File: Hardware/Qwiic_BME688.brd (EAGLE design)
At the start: 25.4 x 25.4 mm, 35 parts, among them J1 DNP, J2 QWIIC_RA, J4 QWIIC_RA

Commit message: Create BME688 eagle footprint and schematic symbol
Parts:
- added U1: BME688LGA, BME688:LGA_8PIN
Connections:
- new net CSB: U1.2
- new net SDO: U1.5
- new net VDD: U1.8
- new net VDDIO: U1.6
- net GND: now also U1.1, U1.7
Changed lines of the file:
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@@
 <element name="U$5" library="output" package="PWR0" value="" x="0.762" y="7.747" smashed="yes"/>
 <element name="U$6" library="output" package="#PWR#0" value="" x="5.715" y="6.35" smashed="yes" rot="MR0"/>
+<element name="U1" library="BME688" package="LGA_8PIN" value="BME688LGA" x="-15.24" y="-10.16" smashed="yes">
+<attribute name="NAME" x="-16.51" y="-12.7" size="0.635" layer="25" font="vector"/>
+<attribute name="VALUE" x="-16.51" y="-7.62" size="0.635" layer="27" font="vector"/>
+</element>
 </elements>
 <signals>
@@
 <contactref element="J1" pad="1"/>
 <via x="1.016" y="6.35" extent="1-16" drill="0.3"/>
+<contactref element="U1" pad="7"/>
+<contactref element="U1" pad="1"/>
 <wire x1="8.89" y1="1.27" x2="20.32" y2="11.2" width="0" layer="19" extent="1-1"/>
 <wire x1="2.298" y1="6.35" x2="8.89" y2="1.27" width="0" layer="19" extent="1-1"/>
 <wire x1="1.016" y1="6.35" x2="2.298" y2="6.35" width="0" layer="19" extent="1-1"/>
 <wire x1="5.08" y1="14.2" x2="2.298" y2="6.35" width="0" layer="19" extent="1-1"/>
+<wire x1="-14.04" y1="-8.96" x2="1.016" y2="6.35" width="0" layer="19" extent="1-1"/>
+<wire x1="-16.44" y1="-9.76" x2="-14.04" y2="-8.96" width="0" layer="19" extent="1-1"/>
 </signal>
 <signal name="SCL">
@@
 <wire x1="16.256" y1="16.598" x2="13.7414" y2="17.78" width="0" layer="19" extent="1-16"/>
 </signal>
+<signal name="CSB">
+<contactref element="U1" pad="2"/>
+</signal>
+<signal name="SDO">
+<contactref element="U1" pad="5"/>
+</signal>
+<signal name="VDDIO">
+<contactref element="U1" pad="6"/>
+</signal>
+<signal name="VDD">
+<contactref element="U1" pad="8"/>
+</signal>
 </signals>

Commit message: Schematic done
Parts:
- added C1, C2: 0.1uF, SparkFun-Capacitors:0402
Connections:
- removed net CSB: U1.2
- removed net SDO: U1.5
- removed net VDD: U1.8
- removed net VDDIO: U1.6
- net 3.3V: now also C1.1, C2.1, U1.2, U1.6, U1.8
- net GND: now also C1.2, C2.2, U1.5
- net SCL: now also U1.4
- net SDA: now also U1.3
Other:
- board text added: "Priyanka Makin"
- board text removed: "Paul Clark"
- board text removed: "Revised by: Priyanka Makin"
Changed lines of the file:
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@@
 <layer number="56" name="wert" color="7" fill="1" visible="no" active="no"/>
 <layer number="57" name="tCAD" color="7" fill="1" visible="no" active="no"/>
+<layer number="58" name="bCopper" color="7" fill="1" visible="no" active="no"/>
 <layer number="59" name="tCarbon" color="7" fill="1" visible="no" active="no"/>
 <layer number="60" name="bCarbon" color="7" fill="1" visible="no" active="no"/>
@@
 <layer number="250" name="Descript" color="3" fill="1" visible="no" active="no"/>
 <layer number="251" name="SMDround" color="12" fill="11" visible="no" active="no"/>
+<layer number="253" name="Extra" color="7" fill="1" visible="no" active="no"/>
 <layer number="254" name="cooling" color="7" fill="1" visible="no" active="no"/>
 <layer number="255" name="routoute" color="7" fill="1" visible="no" active="no"/>
@@
 <dimension x1="0" y1="25.4" x2="25.4" y2="25.4" x3="12.7" y3="34.29" textsize="1.778" textratio="15" layer="47" unit="inch"/>
 <text x="12.7" y="39.37" size="1.778" layer="47" font="vector" ratio="15" align="center">Dimensions in inches</text>
-<text x="76.2" y="-10.16" size="1.778" layer="51" font="vector" ratio="10">Paul Clark</text>
+<text x="76.2" y="-10.16" size="1.778" layer="51" font="vector" ratio="10">Priyanka Makin</text>
 <text x="33.02" y="38.1" size="1.778" layer="51" font="vector" ratio="10" align="top-left">2 Layers
 1.6mm Thickness
 HASL Finish</text>
-<text x="57.15" y="-12.7" size="1.778" layer="51" font="vector" ratio="10">Revised by: Priyanka Makin</text>
 <dimension x1="5.08" y1="12.7" x2="5.08" y2="0" x3="-1.27" y3="6.35" textsize="1.778" textratio="15" layer="47" unit="inch"/>
 <dimension x1="8.89" y1="1.27" x2="0" y2="1.27" x3="4.445" y3="26.67" textsize="1.778" textratio="15" layer="47" unit="inch"/>
@@
 <attribute name="VALUE" x="-16.51" y="-7.62" size="0.635" layer="27" font="vector"/>
 </element>
+<element name="C1" library="SparkFun-Capacitors" package="0402" value="0.1uF" x="-13.97" y="-15.24" smashed="yes">
+<attribute name="NAME" x="-13.97" y="-14.478" size="0.6096" layer="25" font="vector" ratio="20" align="bottom-center"/>
+<attribute name="PROD_ID" value="CAP-12416" x="-13.97" y="-15.24" size="1.778" layer="27" font="vector" ratio="15" display="off"/>
+<attribute name="VALUE" x="-13.97" y="-16.002" size="0.6096" layer="27" font="vector" ratio="20" align="top-center"/>
+</element>
+<element name="C2" library="SparkFun-Capacitors" package="0402" value="0.1uF" x="-13.97" y="-19.05" smashed="yes">
+<attribute name="NAME" x="-13.97" y="-18.288" size="0.6096" layer="25" font="vector" ratio="20" align="bottom-center"/>
+<attribute name="PROD_ID" value="CAP-12416" x="-13.97" y="-19.05" size="1.778" layer="27" font="vector" ratio="15" display="off"/>
+<attribute name="VALUE" x="-13.97" y="-19.812" size="0.6096" layer="27" font="vector" ratio="20" align="top-center"/>
+</element>
 </elements>
 <signals>
@@
 <contactref element="I2C" pad="2"/>
 <wire x1="20.328" y1="12.192" x2="20.32" y2="12.2" width="0.4064" layer="1"/>
+<contactref element="U1" pad="6"/>
+<contactref element="U1" pad="8"/>
+<contactref element="U1" pad="2"/>
+<contactref element="C1" pad="1"/>
+<contactref element="C2" pad="1"/>
 <wire x1="5.08" y1="13.2" x2="12.7" y2="17.78" width="0" layer="19" extent="1-16"/>
 <wire x1="6.0833" y1="6.35" x2="5.08" y2="13.2" width="0" layer="19" extent="1-16"/>
 <wire x1="11.43" y1="1.27" x2="6.0833" y2="6.35" width="0" layer="19" extent="16-16"/>
 <wire x1="20.32" y1="12.2" x2="12.7" y2="17.78" width="0" layer="19" extent="1-16"/>
+<wire x1="-14.04" y1="-9.76" x2="6.0833" y2="6.35" width="0" layer="19" extent="1-16"/>
+<wire x1="-16.44" y1="-10.56" x2="-14.04" y2="-9.76" width="0" layer="19" extent="1-1"/>
+<wire x1="-16.44" y1="-8.96" x2="-16.44" y2="-10.56" width="0" layer="19" extent="1-1"/>
+<wire x1="-14.55" y1="-15.24" x2="-16.44" y2="-10.56" width="0" layer="19" extent="1-1"/>
+<wire x1="-14.55" y1="-19.05" x2="-14.55" y2="-15.24" width="0" layer="19" extent="1-1"/>
 </signal>
 <signal name="GND">
@@
 <contactref element="J1" pad="1"/>
 <via x="1.016" y="6.35" extent="1-16" drill="0.3"/>
+<contactref element="U1" pad="5"/>
 <contactref element="U1" pad="7"/>
 <contactref element="U1" pad="1"/>
+<contactref element="C1" pad="2"/>
+<contactref element="C2" pad="2"/>
 <wire x1="8.89" y1="1.27" x2="20.32" y2="11.2" width="0" layer="19" extent="1-1"/>
 <wire x1="2.298" y1="6.35" x2="8.89" y2="1.27" width="0" layer="19" extent="1-1"/>
@@
 <wire x1="-14.04" y1="-8.96" x2="1.016" y2="6.35" width="0" layer="19" extent="1-1"/>
 <wire x1="-16.44" y1="-9.76" x2="-14.04" y2="-8.96" width="0" layer="19" extent="1-1"/>
+<wire x1="-16.44" y1="-11.36" x2="-16.44" y2="-9.76" width="0" layer="19" extent="1-1"/>
+<wire x1="-13.39" y1="-15.24" x2="-16.44" y2="-11.36" width="0" layer="19" extent="1-1"/>
+<wire x1="-13.39" y1="-19.05" x2="-13.39" y2="-15.24" width="0" layer="19" extent="1-1"/>
 </signal>
 <signal name="SCL">
@@
 <contactref element="R2" pad="1"/>
 <contactref element="J1" pad="4"/>
+<contactref element="U1" pad="4"/>
 <wire x1="16.256" y1="14.898" x2="20.32" y2="14.2" width="0" layer="19" extent="1-1"/>
 <wire x1="5.08" y1="11.2" x2="16.256" y2="14.898" width="0" layer="19" extent="1-1"/>
 <wire x1="16.51" y1="1.27" x2="20.32" y2="14.2" width="0" layer="19" extent="1-1"/>
+<wire x1="-14.04" y1="-11.36" x2="5.08" y2="11.2" width="0" layer="19" extent="1-1"/>
 </signal>
 <signal name="SDA">
@@
 <contactref element="J1" pad="3"/>
 <wire x1="9.144" y1="14.898" x2="9.1349375" y2="14.9070625" width="0.3048" layer="1"/>
+<contactref element="U1" pad="3"/>
 <wire x1="9.144" y1="14.898" x2="20.32" y2="13.2" width="0" layer="19" extent="1-1"/>
 <wire x1="5.08" y1="12.2" x2="9.144" y2="14.898" width="0" layer="19" extent="1-1"/>
 <wire x1="13.97" y1="1.27" x2="20.32" y2="13.2" width="0" layer="19" extent="1-1"/>
+<wire x1="-14.04" y1="-10.56" x2="5.08" y2="12.2" width="0" layer="19" extent="1-1"/>
 </signal>
 <signal name="N$3">
@@
 <wire x1="16.256" y1="16.598" x2="13.7414" y2="17.78" width="0" layer="19" extent="1-16"/>
 </signal>
-<signal name="CSB">
-<contactref element="U1" pad="2"/>
-</signal>
-<signal name="SDO">
-<contactref element="U1" pad="5"/>
-</signal>
-<signal name="VDDIO">
-<contactref element="U1" pad="6"/>
-</signal>
-<signal name="VDD">
-<contactref element="U1" pad="8"/>
-</signal>
 </signals>

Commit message: Updating schematic
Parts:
- added ADR: JUMPER-SMT_3_1-NC_TRACE_SILK, SparkFun-Jumpers:SMT-JUMPER_3_1-NC_TRACE_SILK
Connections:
- new net N$6: ADR.2, U1.5
- net 3.3V: now also ADR.1
- net GND: now also ADR.3; no longer U1.5
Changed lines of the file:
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@@
 <attribute name="VALUE" x="-13.97" y="-19.812" size="0.6096" layer="27" font="vector" ratio="20" align="top-center"/>
+</element>
+<element name="ADR" library="SparkFun-Jumpers" package="SMT-JUMPER_3_1-NC_TRACE_SILK" package3d_urn="urn:adsk.eagle:package:39288/1" value="JUMPER-SMT_3_1-NC_TRACE_SILK" x="-19.05" y="-17.78" smashed="yes">
+<attribute name="NAME" x="-19.05" y="-16.637" size="0.6096" layer="25" font="vector" ratio="20" align="bottom-center"/>
+<attribute name="VALUE" x="-19.05" y="-18.923" size="0.6096" layer="27" font="vector" ratio="20" align="top-center"/>
 </element>
 </elements>
@@
 <contactref element="C1" pad="1"/>
 <contactref element="C2" pad="1"/>
-<wire x1="5.08" y1="13.2" x2="12.7" y2="17.78" width="0" layer="19" extent="1-16"/>
-<wire x1="6.0833" y1="6.35" x2="5.08" y2="13.2" width="0" layer="19" extent="1-16"/>
+<contactref element="ADR" pad="1"/>
+<wire x1="-14.55" y1="-19.05" x2="-20.0914" y2="-17.78" width="0" layer="19" extent="1-1"/>
+<wire x1="-14.55" y1="-15.24" x2="-14.55" y2="-19.05" width="0" layer="19" extent="1-1"/>
+<wire x1="-16.44" y1="-10.56" x2="-14.55" y2="-15.24" width="0" layer="19" extent="1-1"/>
+<wire x1="-16.44" y1="-8.96" x2="-16.44" y2="-10.56" width="0" layer="19" extent="1-1"/>
+<wire x1="-14.04" y1="-9.76" x2="-16.44" y2="-10.56" width="0" layer="19" extent="1-1"/>
+<wire x1="6.0833" y1="6.35" x2="-14.04" y2="-9.76" width="0" layer="19" extent="1-16"/>
+<wire x1="5.08" y1="13.2" x2="6.0833" y2="6.35" width="0" layer="19" extent="1-16"/>
 <wire x1="11.43" y1="1.27" x2="6.0833" y2="6.35" width="0" layer="19" extent="16-16"/>
+<wire x1="12.7" y1="17.78" x2="5.08" y2="13.2" width="0" layer="19" extent="1-16"/>
 <wire x1="20.32" y1="12.2" x2="12.7" y2="17.78" width="0" layer="19" extent="1-16"/>
-<wire x1="-14.04" y1="-9.76" x2="6.0833" y2="6.35" width="0" layer="19" extent="1-16"/>
-<wire x1="-16.44" y1="-10.56" x2="-14.04" y2="-9.76" width="0" layer="19" extent="1-1"/>
-<wire x1="-16.44" y1="-8.96" x2="-16.44" y2="-10.56" width="0" layer="19" extent="1-1"/>
-<wire x1="-14.55" y1="-15.24" x2="-16.44" y2="-10.56" width="0" layer="19" extent="1-1"/>
-<wire x1="-14.55" y1="-19.05" x2="-14.55" y2="-15.24" width="0" layer="19" extent="1-1"/>
 </signal>
 <signal name="GND">
@@
 <contactref element="J1" pad="1"/>
 <via x="1.016" y="6.35" extent="1-16" drill="0.3"/>
-<contactref element="U1" pad="5"/>
+<contactref element="C1" pad="2"/>
+<contactref element="C2" pad="2"/>
+<contactref element="ADR" pad="3"/>
 <contactref element="U1" pad="7"/>
 <contactref element="U1" pad="1"/>
-<contactref element="C1" pad="2"/>
-<contactref element="C2" pad="2"/>
-<wire x1="8.89" y1="1.27" x2="20.32" y2="11.2" width="0" layer="19" extent="1-1"/>
-<wire x1="2.298" y1="6.35" x2="8.89" y2="1.27" width="0" layer="19" extent="1-1"/>
-<wire x1="1.016" y1="6.35" x2="2.298" y2="6.35" width="0" layer="19" extent="1-1"/>
+<wire x1="-13.39" y1="-19.05" x2="-18.0086" y2="-17.78" width="0" layer="19" extent="1-1"/>
+<wire x1="-13.39" y1="-15.24" x2="-13.39" y2="-19.05" width="0" layer="19" extent="1-1"/>
+<wire x1="-16.44" y1="-9.76" x2="-13.39" y2="-15.24" width="0" layer="19" extent="1-1"/>
+<wire x1="-14.04" y1="-8.96" x2="-16.44" y2="-9.76" width="0" layer="19" extent="1-1"/>
+<wire x1="1.016" y1="6.35" x2="-14.04" y2="-8.96" width="0" layer="19" extent="1-1"/>
+<wire x1="2.298" y1="6.35" x2="1.016" y2="6.35" width="0" layer="19" extent="1-1"/>
 <wire x1="5.08" y1="14.2" x2="2.298" y2="6.35" width="0" layer="19" extent="1-1"/>
-<wire x1="-14.04" y1="-8.96" x2="1.016" y2="6.35" width="0" layer="19" extent="1-1"/>
-<wire x1="-16.44" y1="-9.76" x2="-14.04" y2="-8.96" width="0" layer="19" extent="1-1"/>
-<wire x1="-16.44" y1="-11.36" x2="-16.44" y2="-9.76" width="0" layer="19" extent="1-1"/>
-<wire x1="-13.39" y1="-15.24" x2="-16.44" y2="-11.36" width="0" layer="19" extent="1-1"/>
-<wire x1="-13.39" y1="-19.05" x2="-13.39" y2="-15.24" width="0" layer="19" extent="1-1"/>
+<wire x1="8.89" y1="1.27" x2="2.298" y2="6.35" width="0" layer="19" extent="1-1"/>
+<wire x1="20.32" y1="11.2" x2="8.89" y2="1.27" width="0" layer="19" extent="1-1"/>
 </signal>
 <signal name="SCL">
@@
 <wire x1="16.256" y1="16.598" x2="13.7414" y2="17.78" width="0" layer="19" extent="1-16"/>
 </signal>
+<signal name="N$6">
+<contactref element="U1" pad="5"/>
+<contactref element="ADR" pad="2"/>
+<wire x1="-16.44" y1="-11.36" x2="-19.05" y2="-17.78" width="0" layer="19" extent="1-1"/>
+</signal>
 </signals>

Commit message: Board routed
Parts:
- C1, C2: device SparkFun-Capacitors:0402 -> SparkFun-Capacitors:0603
- moved C2 42.0 mm to (10.2, 15.3), turned to 90 degrees
- moved ADR 40.5 mm to (11.4, 8.89), flipped to the bottom, turned to 180 degrees
- moved U1 36.1 mm to (12.7, 12.7)
- moved C1 35.8 mm to (8.89, 12.3), turned to 180 degrees
- moved R1 8.98 mm to (18.0, 17.0)
- moved I2C 5.12 mm to (17.1, 20.3), turned to 180 degrees
- moved R2 1.27 mm to (16.3, 17.0)
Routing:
- net 3.3V: track 0.01 -> 57.4 mm, vias 0 -> 3
- net SDA: track 0.01 -> 38.8 mm, vias 0 -> 2
- net SCL: track 0.00 -> 35.4 mm, vias 0 -> 3
- net N$1: track 0.00 -> 2.95 mm, vias 0 -> 1
- net N$6: track 0.00 -> 2.64 mm, vias 0 -> 1
- net N$4: track 0.00 -> 2.52 mm, vias 0 -> 1
- net N$2: track 0.00 -> 2.52 mm, vias 0 -> 1

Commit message: Buzzard labels
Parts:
- added U$10, U$7: (no value), output:GAS_SENSOR_#_BME6880
- added U$11: (no value), output:#ADR#0
- added U$9: (no value), output:ADR#_0X760
- moved U$15 5.06 mm to (19.1, 18.3)
- moved LOGO4 3.94 mm to (7.11, 23.9)
- moved LOGO3 2.97 mm to (13.7, 23.1)
- moved LOGO2 0.40 mm to (22.6, 17.4)
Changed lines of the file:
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@@
 <?xml version="1.0" encoding="utf-8"?>
 <!DOCTYPE eagle SYSTEM "eagle.dtd">
-<eagle version="9.5.2">
+<eagle version="9.6.2">
 <drawing>
 <settings>
-<setting alwaysvectorfont="no"/>
+<setting alwaysvectorfont="yes"/>
 <setting keepoldvectorfont="yes"/>
 <setting verticaltext="up"/>
@@
 <layer number="19" name="Unrouted" color="6" fill="1" visible="yes" active="yes"/>
 <layer number="20" name="Dimension" color="24" fill="1" visible="yes" active="yes"/>
-<layer number="21" name="tPlace" color="16" fill="1" visible="yes" active="yes"/>
+<layer number="21" name="tPlace" color="16" fill="1" visible="no" active="yes"/>
 <layer number="22" name="bPlace" color="14" fill="1" visible="yes" active="yes"/>
 <layer number="23" name="tOrigins" color="15" fill="1" visible="yes" active="yes"/>
@@
 <attribute name="NAME" x="17.145" y="19.177" size="0.6096" layer="26" font="vector" ratio="20" rot="MR180" align="bottom-center"/>
 </element>
-<element name="U$15" library="SparkFun-Buzzard" package="I2C" value="" x="14.605" y="15.875" smashed="yes" rot="MR0"/>
+<element name="U$15" library="SparkFun-Buzzard" package="I2C" value="" x="19.05" y="18.288" smashed="yes" rot="MR0"/>
 <element name="LOGO1" library="SparkFun-Aesthetics" package="ORDERING_INSTRUCTIONS" value="SPECIAL_INSTRUCTIONS-ORDERING" x="30.48" y="50.8" smashed="yes"/>
 <element name="U$33" library="output" package="#GND#0" value="" x="8.89" y="3.937" smashed="yes" rot="R90"/>
@@
 <element name="U$3" library="output" package="#SDA#0" value="" x="13.97" y="1.778" smashed="yes" rot="MR90"/>
 <element name="U$4" library="output" package="#SCL#0" value="" x="16.51" y="1.778" smashed="yes" rot="MR90"/>
-<element name="LOGO2" library="SparkFun-Aesthetics" package="QWIIC_5MM" value="QWIIC_LOGO_5MM" x="22.479" y="17.78" smashed="yes"/>
-<element name="LOGO3" library="SparkFun-Aesthetics" package="SFE_LOGO_NAME_.1" value="SFE_LOGO_NAME.1_INCH" x="12.7" y="20.32" smashed="yes" rot="MR0"/>
-<element name="LOGO4" library="SparkFun-Aesthetics" package="SFE_LOGO_FLAME_.1" value="SFE_LOGO_FLAME.1_INCH" x="10.922" y="22.86" smashed="yes" rot="MR0"/>
+<element name="LOGO2" library="SparkFun-Aesthetics" package="QWIIC_5MM" value="QWIIC_LOGO_5MM" x="22.606" y="17.399" smashed="yes"/>
+<element name="LOGO3" library="SparkFun-Aesthetics" package="SFE_LOGO_NAME_.1" value="SFE_LOGO_NAME.1_INCH" x="13.716" y="23.114" smashed="yes" rot="MR0"/>
+<element name="LOGO4" library="SparkFun-Aesthetics" package="SFE_LOGO_FLAME_.1" value="SFE_LOGO_FLAME.1_INCH" x="7.112" y="23.876" smashed="yes" rot="MR0"/>
 <element name="LOGO6" library="SparkFun-Aesthetics" package="SFE_LOGO_NAME_.1" value="SFE_LOGO_NAME.1_INCH" x="12.7" y="23.368" smashed="yes"/>
 <element name="JP7" library="SparkFun-Hardware" package="STAND-OFF" value="STAND-OFF" x="22.86" y="2.54" smashed="yes">
@@
 <attribute name="VALUE" x="11.43" y="10.033" size="0.6096" layer="28" font="vector" ratio="20" rot="MR180" align="top-center"/>
 </element>
+<element name="U$9" library="output" package="ADR#_0X760" value="" x="8.255" y="19.939" smashed="yes"/>
+<element name="U$10" library="output" package="GAS_SENSOR_#_BME6880" value="" x="4.445" y="21.336" smashed="yes"/>
+<element name="U$11" library="output" package="#ADR#0" value="" x="10.16" y="8.89" smashed="yes" rot="MR0"/>
+<element name="U$7" library="output" package="GAS_SENSOR_#_BME6880" value="" x="20.32" y="13.97" smashed="yes" rot="MR0"/>
 </elements>
 <signals>

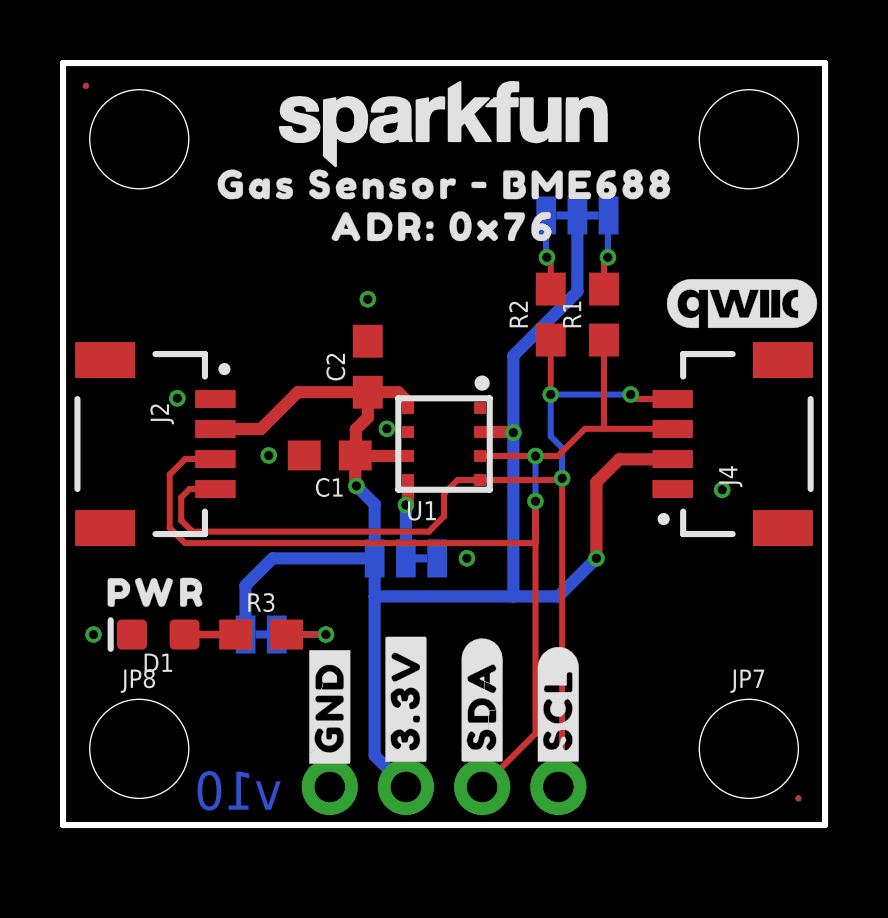
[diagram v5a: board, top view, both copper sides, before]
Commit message: Design review updates
Schematic:
* Add headers for CSB and SDO
* Add NC jumper between CSB and 3.3V
* Add 10k resistor for 3-way jumper
* Replace I2C pullups with 2.2kohms
* Increase the size of fiducials
Board:
* Change version number to v01
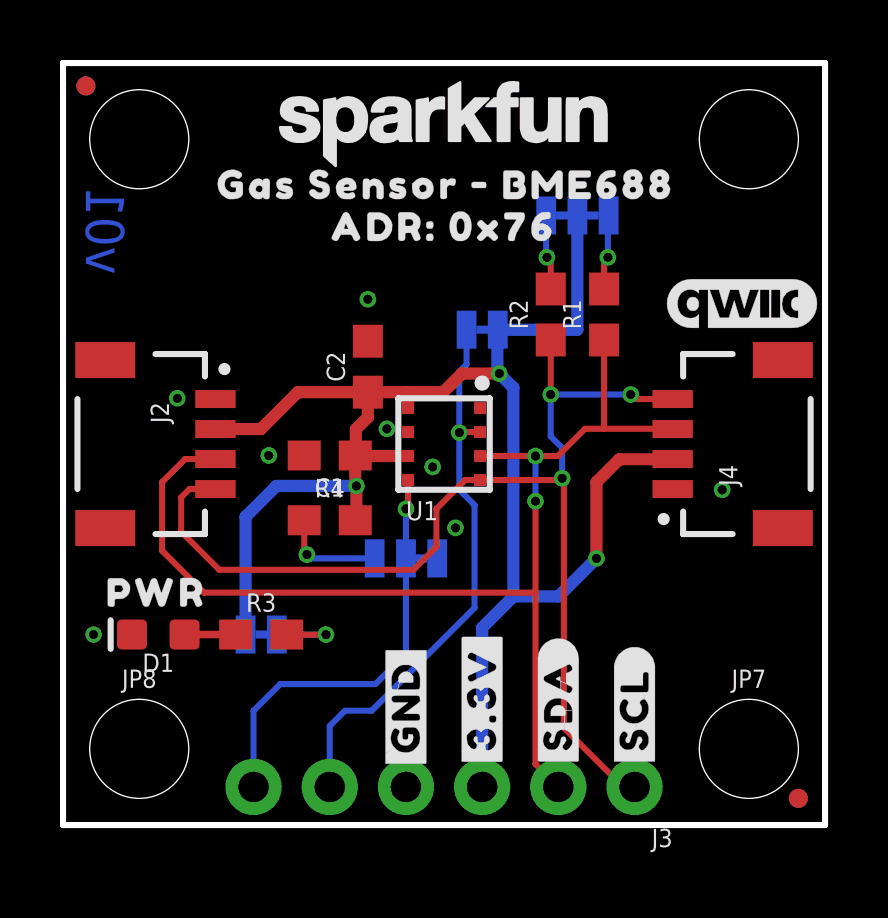
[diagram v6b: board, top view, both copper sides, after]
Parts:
- removed J1: DNP, SparkFun-Connectors:1X04_NO_SILK
- added CSB: JUMPER-SMT_2_NC_TRACE_SILK, SparkFun-Jumpers:SMT-JUMPER_2_NC_TRACE_SILK
- added J3: (no value), SparkFun-Connectors:1X06_NO_SILK
- added R4: 10k, SparkFun-Resistors:0603
- JP1, JP2, JP5, JP6: value FIDUCIAL0.2MM -> FIDUCIALUFIDUCIAL; device SparkFun-Aesthetics:FIDUCIAL-0.2MM -> SparkFun-Aesthetics:FIDUCIAL-MICRO
- R1, R2: value 4.7k -> 2.2k
- moved U$2 2.54 mm to (14.0, 4.19)
- moved U$3 2.54 mm to (16.5, 1.78)
- moved U$34 2.54 mm to (14.0, 4.19)
- moved U$35 2.54 mm to (16.5, 1.78)
- moved U$1 2.54 mm to (11.4, 3.94)
- moved U$33 2.54 mm to (11.4, 3.94)
- moved U$36 2.54 mm to (19.1, 1.78)
- moved U$4 2.54 mm to (19.1, 1.78)
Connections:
- removed net N$6: ADR.2, U1.5
- new net CSB: CSB.2, J3.5, U1.2
- new net N$5: ADR.1, R4.1
- new net SDO: ADR.2, J3.6, U1.5
- net 3.3V: now also CSB.1, J3.3, R4.2; no longer ADR.1, J1.2, U1.2
- net GND: now also J3.4; no longer J1.1
- net SCL: now also J3.1; no longer J1.4
- net SDA: now also J3.2; no longer J1.3
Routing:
- net CSB: track 0.00 -> 18.8 mm, vias 0 -> 1
- net SDO: track 0.00 -> 14.2 mm, vias 0 -> 1
- net N$5: track 0.00 -> 3.49 mm, vias 0 -> 1
- net SCL: track 35.4 -> 38.1 mm
- net N$6: track 2.64 -> 0.00 mm, vias 1 -> 0
- net 3.3V: track 57.4 -> 56.2 mm
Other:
- board text added: "2 Layers 1.6mm Thickness HASL lead-free Finish"
- board text added: "v01"
- board text removed: "2 Layers 1.6mm Thickness HASL Finish"
- board text removed: "v10"
